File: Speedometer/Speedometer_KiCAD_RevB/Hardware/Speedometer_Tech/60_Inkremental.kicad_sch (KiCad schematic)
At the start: 2 parts

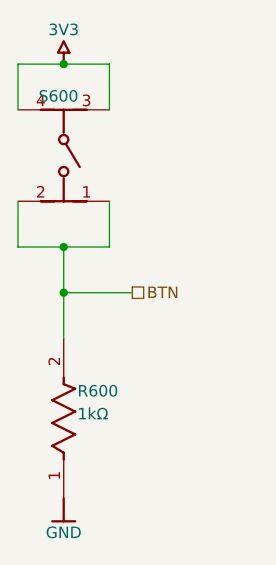
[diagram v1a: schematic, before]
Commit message: current version of lada speedometer in kicad
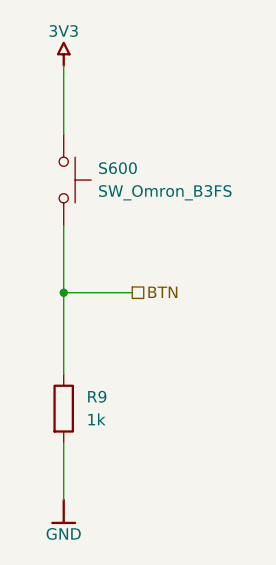
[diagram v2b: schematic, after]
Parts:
- removed R600: 1kΩ, FP-CRCW0603-e3-MFG, symbol Speedometer_Tech-altium-import:Designator_1_1029c3af85768c4190bb7ad29bc67b5
- removed S600: ~, FP-PTS645SM43SMTR92LFS-MFG, symbol Speedometer_Tech-altium-import:Designator_3_1adf0dd01260c80cf25a44bfd6b99ba
- added R9: 1k, Resistor_SMD:R_0603_1608Metric, symbol Device:R
- added S600: SW_Omron_B3FS, Button_Switch_SMD:SW_SPST_Omron_B3FS-100xP, symbol Switch:SW_Omron_B3FS
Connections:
- net 3V3: now also S600.1
- net BTN: now also R9.1, S600.2
- net GND: now also R9.2
